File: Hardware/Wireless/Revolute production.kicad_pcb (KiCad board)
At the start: 4 copper layers, 19.9 x 19.5 mm, 58 parts, among them J1 -, J2 +, Q1 NMOS-CSD17381F4, Q2 NMOS-CSD17381F4, Q3 PMOS-CSD25483F4, Q4 PMOS-CSD25483F4, Q5 PMOS-CSD25483F4, SW1 SW_Omron_B3FS, U10 BQ24075RGT, U11 MIC5504, U5 BQ27427, U6 nrf52833_qfn40, U8 Conn_01x14_Socket, U9 AS5600, X1 32.768 kHz, X2 32MHZ

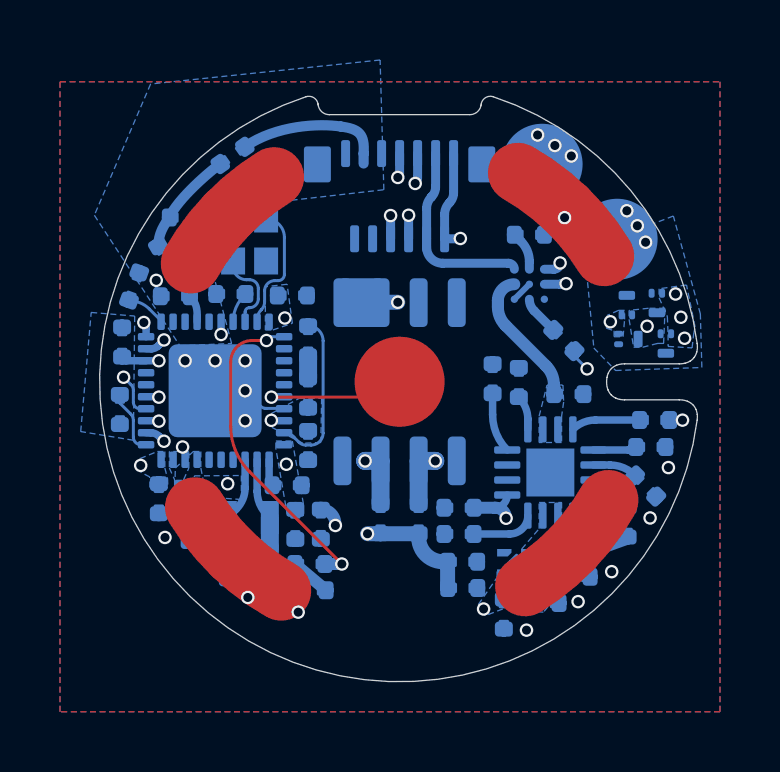
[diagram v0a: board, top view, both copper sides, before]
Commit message: added status led
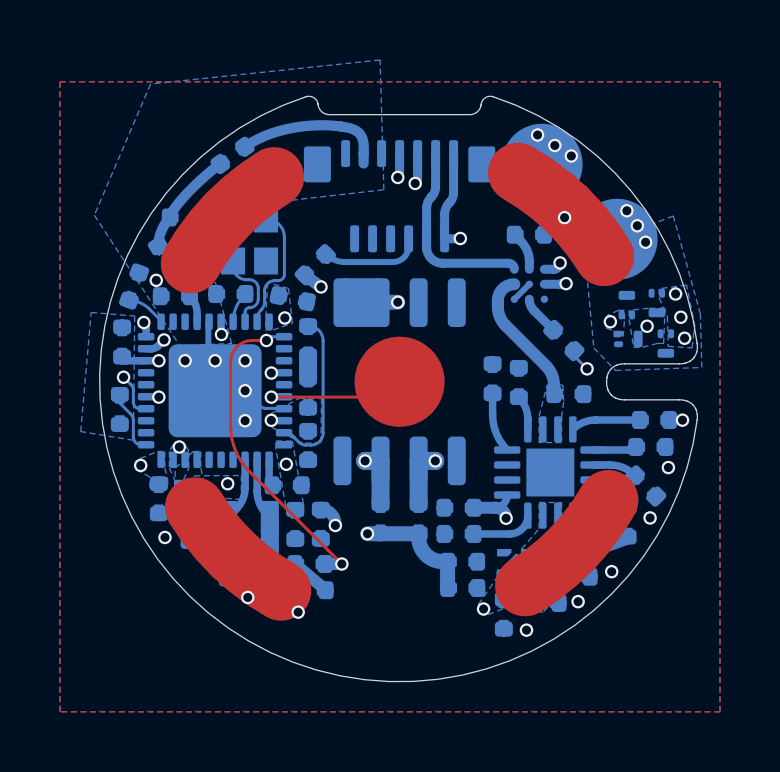
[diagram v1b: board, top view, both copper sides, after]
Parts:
- added R12: 1.5k, Library:0402, B.Cu at (147.2, 96.1)
- moved C11 0.11 mm to (146.4, 97.2), turned to -12 degrees
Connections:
- U6 pad 12: D- -> unconnected-(U6-D--Pad12)
- U6 pad 13: D+ -> unconnected-(U6-D+-Pad13)
- U6 pad 34: P0.29 -> FLEX_LED
- U8 pad 6: D+ -> unconnected-(U8-Pin_6-Pad6)
- U8 pad 8: D- -> Net-(U8-Pin_8)
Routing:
- net D-: track 14.9 -> 0.00 mm, vias 2 -> 0
- net D+: track 14.7 -> 0.00 mm, vias 2 -> 0
- net FLEX_LED: track 0.00 -> 4.55 mm, vias 0 -> 2
- net Net-(U8-Pin_8): track 0.00 -> 3.35 mm
- net GND: track 3.75 -> 6.18 mm

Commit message: revolute production boards
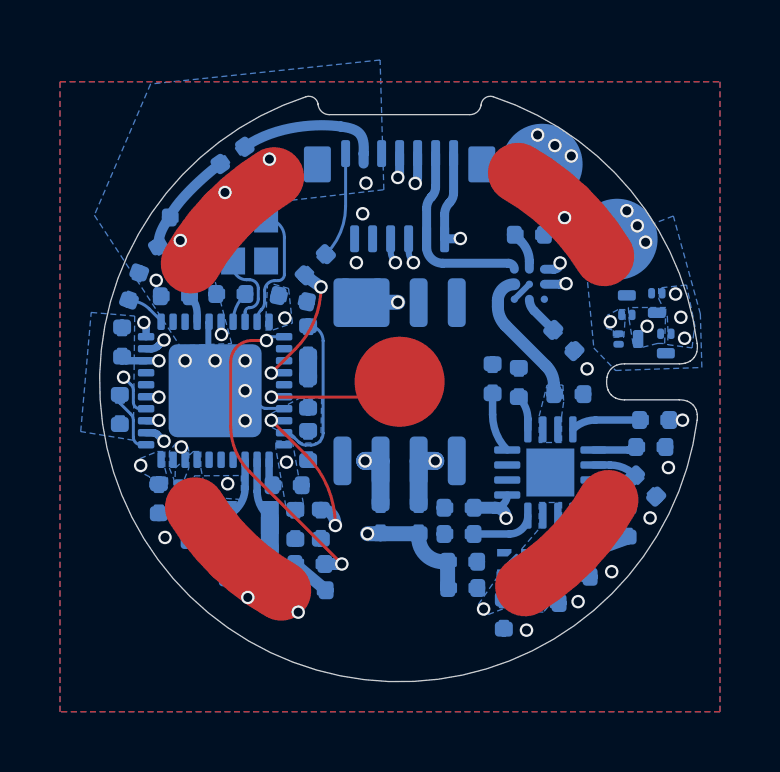
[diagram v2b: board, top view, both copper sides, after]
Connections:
- R12 pad 1: Net-(U8-Pin_8) -> Net-(U8-Pin_1)
- U6 pad 12: unconnected-(U6-D--Pad12) -> D-
- U6 pad 13: unconnected-(U6-D+-Pad13) -> D+
- U8 pad 1: GND -> Net-(U8-Pin_1)
- U8 pad 6: unconnected-(U8-Pin_6-Pad6) -> D+
- U8 pad 8: Net-(U8-Pin_8) -> D-
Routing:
- net D-: track 0.00 -> 12.6 mm, vias 0 -> 2
- net D+: track 0.00 -> 11.2 mm, vias 0 -> 2
- net P0.15: track 23.8 -> 13.4 mm
- net Net-(U8-Pin_1): track 0.00 -> 3.52 mm
- net Net-(U8-Pin_8): track 3.35 -> 0.00 mm
- net P0.17: track 24.1 -> 21.9 mm
- net GND: track 6.18 -> 5.41 mm, vias 18 -> 24
- net swd: track 13.4 -> 12.8 mm
